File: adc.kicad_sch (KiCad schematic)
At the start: 18 parts, among them U6 ADS1120-PW

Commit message: maj puissance
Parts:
- renumbered CDiff1 to CDi1, CDiff2 to CDi2
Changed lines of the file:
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@@
 		(dnp no)
 		(fields_autoplaced yes)
-		(property "Reference" "CDiff1"
+		(property "Reference" "CDi1"
 			(at 78.74 115.5762 0)
 			(show_name no)
@@
 			(project "OPC V2"
 				(path "/8b16e532-0286-4593-b60d-4fadd60abb3b"
-					(reference "CDiff1")
+					(reference "CDi1")
 					(unit 1)
 				)
@@
 		(dnp no)
 		(fields_autoplaced yes)
-		(property "Reference" "CDiff2"
+		(property "Reference" "CDi2"
 			(at 78.74 64.7762 0)
 			(show_name no)
@@
 			(project "OPC V2"
 				(path "/8b16e532-0286-4593-b60d-4fadd60abb3b"
-					(reference "CDiff2")
+					(reference "CDi2")
 					(unit 1)
 				)

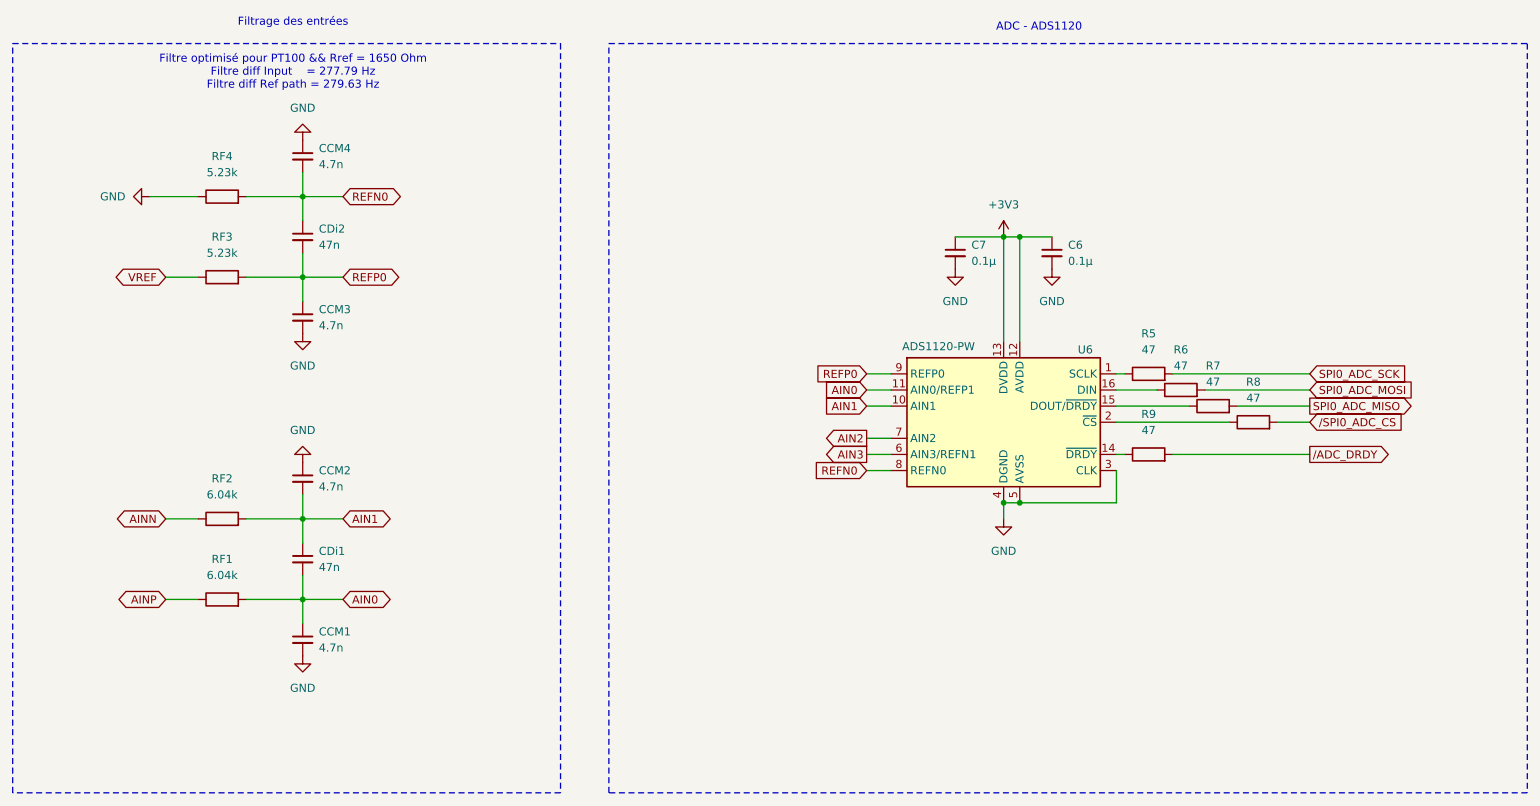
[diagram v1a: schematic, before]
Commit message: découpage et hierarchie
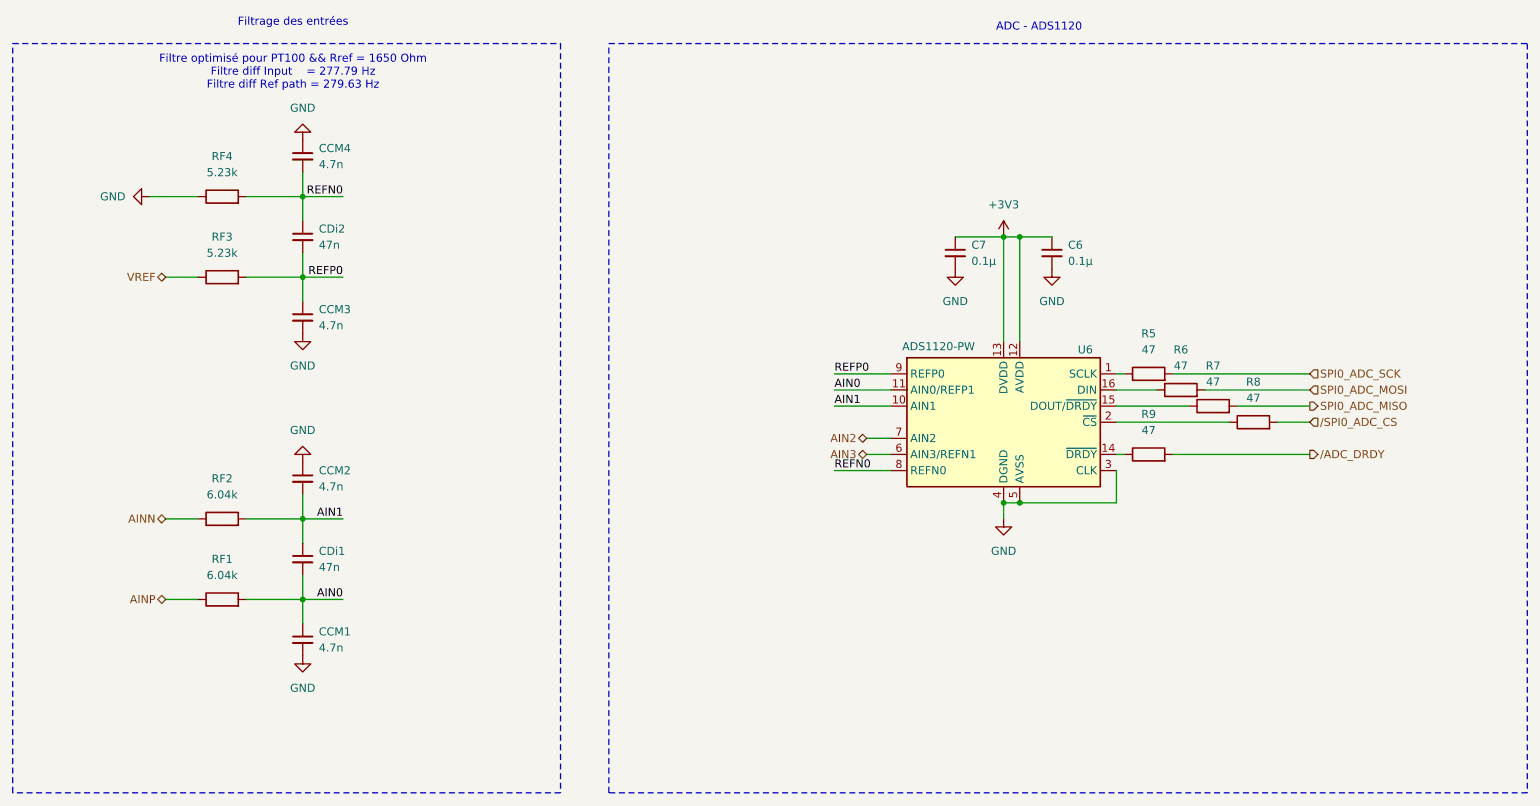
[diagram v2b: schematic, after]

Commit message: suite et nouvel écran
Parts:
- renumbered C6 to C4, C7 to C5, R7 to R10, R9 to R11, R8 to R12, R5 to R13, R6 to R8, U6 to U5
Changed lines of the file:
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@@
 		(dnp no)
 		(fields_autoplaced yes)
-		(property "Reference" "R7"
+		(property "Reference" "R10"
 			(at 219.71 86.36 90)
 			(show_name no)
@@
 			(project "OPC V2"
 				(path "/594181e6-a34f-458c-9685-d994528736df/4e7d77c0-f089-449f-bb85-d9c53540b599"
-					(reference "R7")
+					(reference "R10")
 					(unit 1)
 				)
@@
 		(in_pos_files yes)
 		(dnp no)
-		(property "Reference" "U6"
+		(property "Reference" "U5"
 			(at 198.374 83.82 0)
 			(show_name no)
@@
 			(project "OPC V2"
 				(path "/594181e6-a34f-458c-9685-d994528736df/4e7d77c0-f089-449f-bb85-d9c53540b599"
-					(reference "U6")
+					(reference "U5")
 					(unit 1)
 				)
@@
 		(dnp no)
 		(fields_autoplaced yes)
-		(property "Reference" "R5"
+		(property "Reference" "R13"
 			(at 209.55 81.28 90)
 			(show_name no)
@@
 			(project "OPC V2"
 				(path "/594181e6-a34f-458c-9685-d994528736df/4e7d77c0-f089-449f-bb85-d9c53540b599"
-					(reference "R5")
+					(reference "R13")
 					(unit 1)
 				)
@@
 		(dnp no)
 		(fields_autoplaced yes)
-		(property "Reference" "R8"
+		(property "Reference" "R12"
 			(at 226.06 88.9 90)
 			(show_name no)
@@
 			(project "OPC V2"
 				(path "/594181e6-a34f-458c-9685-d994528736df/4e7d77c0-f089-449f-bb85-d9c53540b599"
-					(reference "R8")
+					(reference "R12")
 					(unit 1)
 				)
@@
 		(dnp no)
 		(fields_autoplaced yes)
-		(property "Reference" "R6"
+		(property "Reference" "R8"
 			(at 214.63 83.82 90)
 			(show_name no)
@@
 			(project "OPC V2"
 				(path "/594181e6-a34f-458c-9685-d994528736df/4e7d77c0-f089-449f-bb85-d9c53540b599"
-					(reference "R6")
+					(reference "R8")
 					(unit 1)
 				)
@@
 		(dnp no)
 		(fields_autoplaced yes)
-		(property "Reference" "C6"
+		(property "Reference" "C4"
 			(at 196.85 67.3162 0)
 			(show_name no)
@@
 			(project "OPC V2"
 				(path "/594181e6-a34f-458c-9685-d994528736df/4e7d77c0-f089-449f-bb85-d9c53540b599"
-					(reference "C6")
+					(reference "C4")
 					(unit 1)
 				)
@@
 		(dnp no)
 		(fields_autoplaced yes)
-		(property "Reference" "C7"
+		(property "Reference" "C5"
 			(at 181.61 67.3162 0)
 			(show_name no)
@@
 			(project "OPC V2"
 				(path "/594181e6-a34f-458c-9685-d994528736df/4e7d77c0-f089-449f-bb85-d9c53540b599"
-					(reference "C7")
+					(reference "C5")
 					(unit 1)
 				)
@@
 		(dnp no)
 		(fields_autoplaced yes)
-		(property "Reference" "R9"
+		(property "Reference" "R11"
 			(at 209.55 93.98 90)
 			(show_name no)
@@
 			(project "OPC V2"
 				(path "/594181e6-a34f-458c-9685-d994528736df/4e7d77c0-f089-449f-bb85-d9c53540b599"
-					(reference "R9")
-					(unit 1)
-				)
+					(reference "R11")
+					(unit 1)
+				)

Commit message: daily
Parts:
- C4, C5: value 0.1µ -> 0.1µ 10V; MF (none) -> Würth Elektronik; MPN (none) -> 885012206020; px_x1 (none) -> 0,095; px_x10 (none) -> 0.031
- CCM1, CCM2, CCM3, CCM4: value 4.7n -> 4.7n C0G; MF (none) -> Murata; MPN (none) -> GCM1885C1H472JA16J; px_x1 (none) -> 0.129; px_x10 (none) -> 0,051
- CDi1, CDi2: value 47n -> 47n C0G; MF (none) -> Murata; MPN (none) -> GRM3195C1H473JA05D; px_x1 (none) -> 0.327; px_x10 (none) -> 0,143
- R10, R11, R12, R13, R8: MF (none) -> Panasonic; MPN (none) -> ERJ-3GEYJ470V; px_x1 (none) -> 0,086; px_x10 (none) -> 0.02
- RF1, RF2: MF (none) -> Panasonic; MPN (none) -> ERA-3AED6041V; px_x1 (none) -> 0.086; px_x10 (none) -> 0,052
- RF3, RF4: MF (none) -> Panasonic; MPN (none) -> ERA-3AEB5231V; px_x1 (none) -> 0,198; px_x10 (none) -> 0,104
- U5: MF (none) -> Texas Instruments; MPN (none) -> ADS1120IPWR; px_x1 (none) -> 6,25; px_x10 (none) -> 4.82
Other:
- title: (none) -> ADC

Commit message: daily
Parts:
- CCM1, CCM2, CCM3, CCM4: value 4.7n C0G -> 4.7n
- CDi1, CDi2: value 47n C0G -> 47n
- renumbered R8 to R1, R13 to R11, R10 to R4, R11 to R6, R12 to R8

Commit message: avant prod
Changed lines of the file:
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@@
 	(wire
 		(pts
-			(xy 160.02 87.63) (xy 168.91 87.63)
+			(xy 158.75 87.63) (xy 168.91 87.63)
 		)
 		(stroke
@@
 	(wire
 		(pts
-			(xy 160.02 102.87) (xy 168.91 102.87)
+			(xy 158.75 102.87) (xy 168.91 102.87)
 		)
 		(stroke
@@
 	)
 	(label "REFN0"
-		(at 160.02 102.87 0)
-		(effects
-			(font
-				(size 1.27 1.27)
-			)
-			(justify left bottom)
+		(at 158.75 102.87 180)
+		(effects
+			(font
+				(size 1.27 1.27)
+			)
+			(justify right bottom)
 		)
 	)
@@
 	)
 	(label "REFP0"
-		(at 160.02 87.63 0)
-		(effects
-			(font
-				(size 1.27 1.27)
-			)
-			(justify left bottom)
-		)
-	)
+		(at 158.75 87.63 180)
+		(effects
+			(font
+				(size 1.27 1.27)
+			)
+			(justify right bottom)
+		)
+	)
